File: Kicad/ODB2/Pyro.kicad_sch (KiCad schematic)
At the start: 35 parts

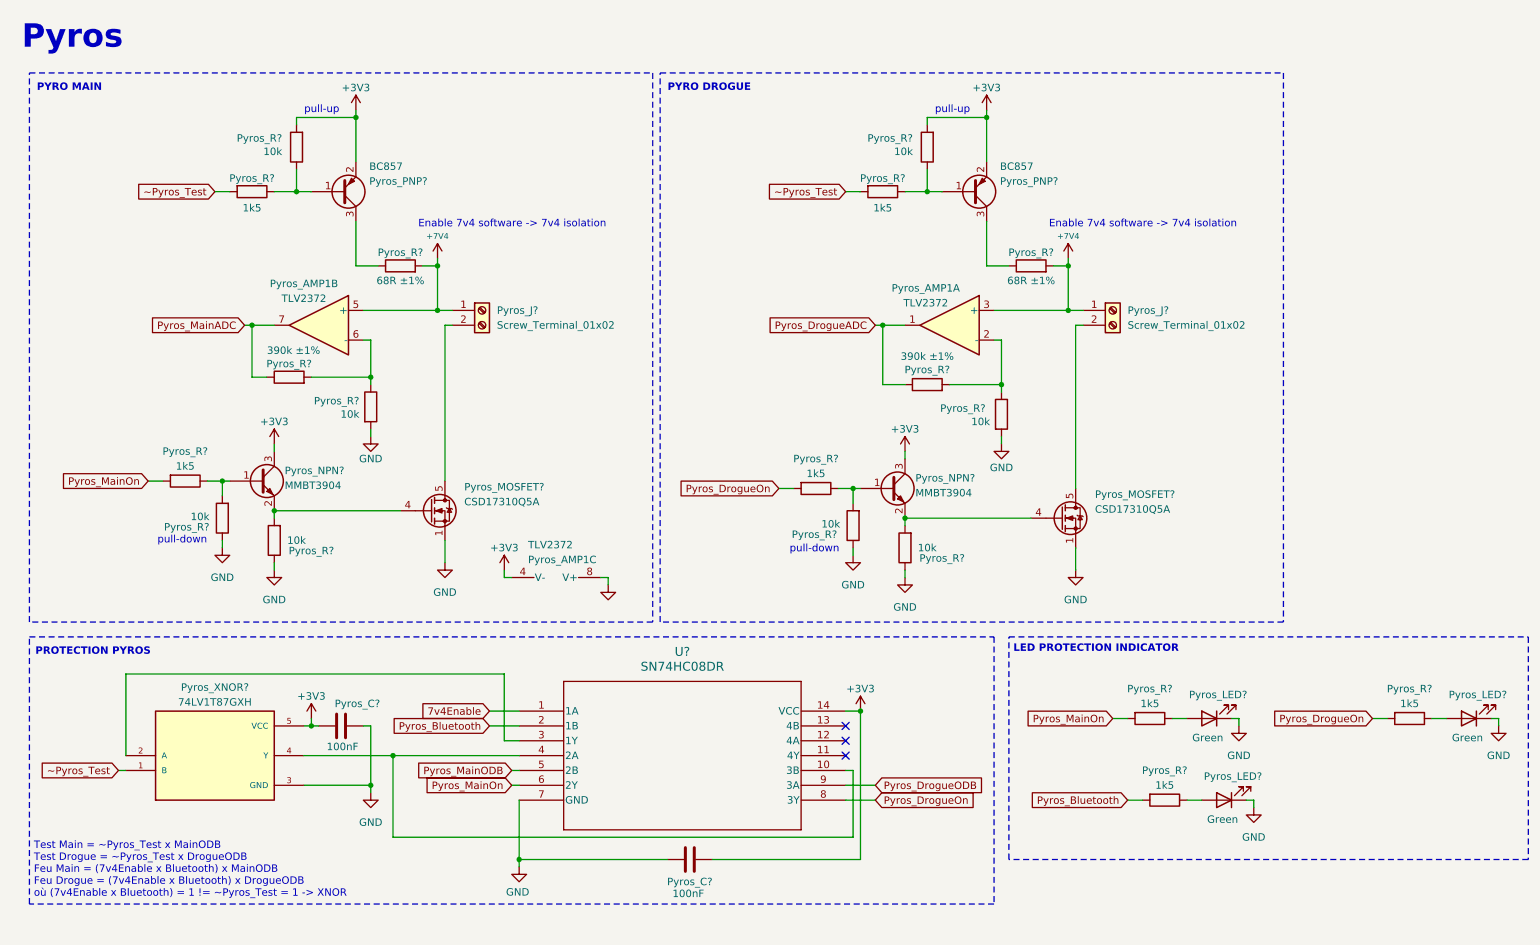
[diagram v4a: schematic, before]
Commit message: fix Labels + fix STM32 projet pinout
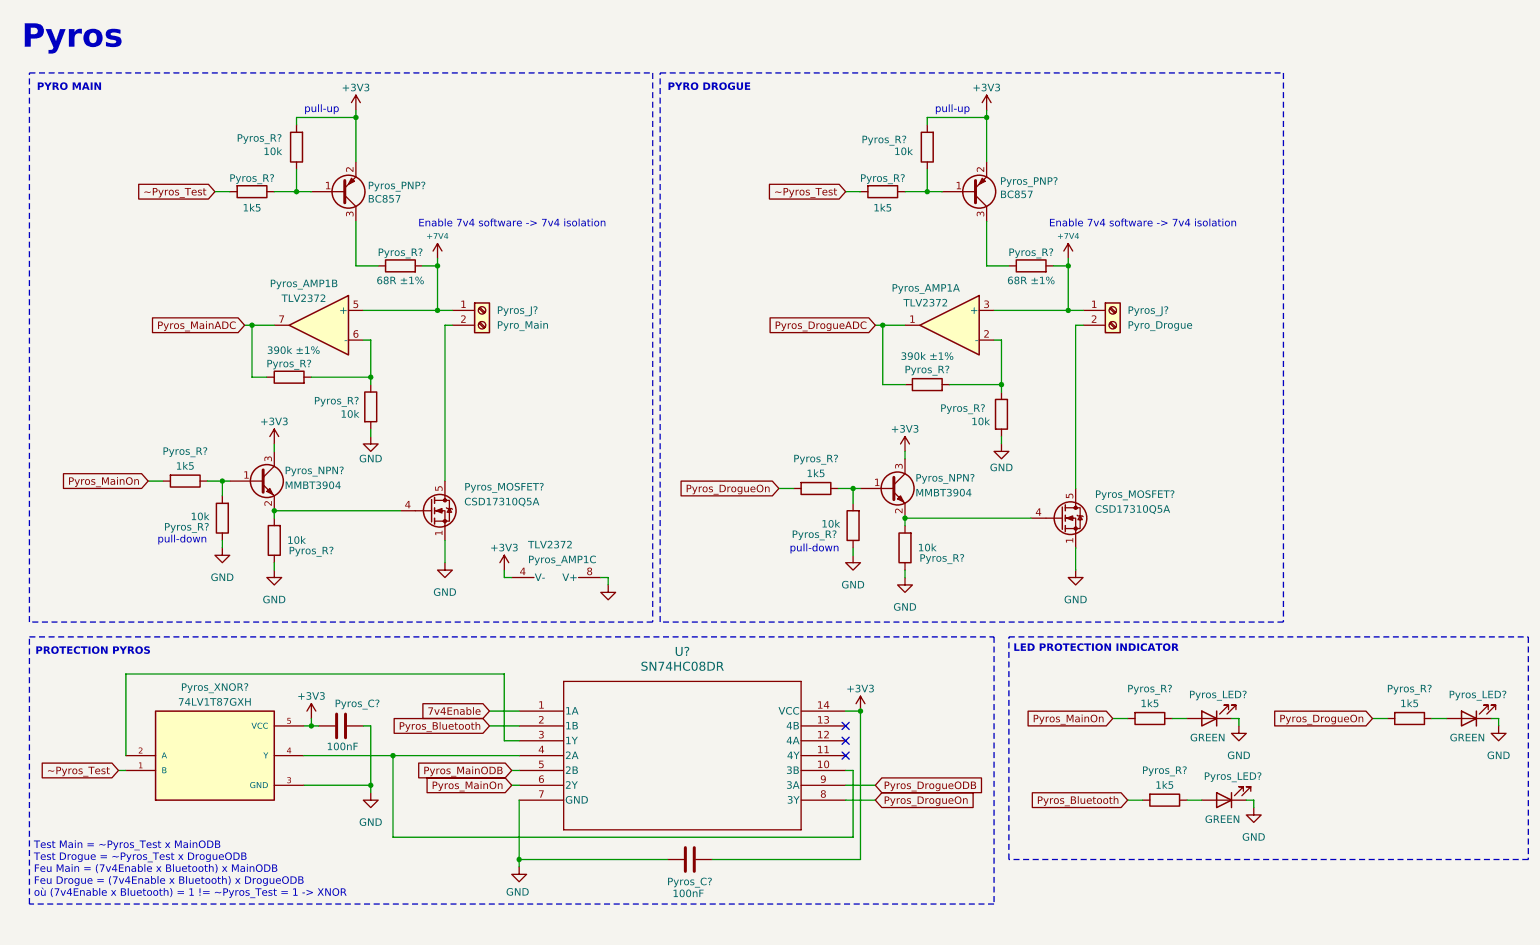
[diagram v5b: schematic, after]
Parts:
- Pyros_J?: value Screw_Terminal_01x02 -> Pyro_Drogue
- Pyros_J?: value Screw_Terminal_01x02 -> Pyro_Main
- Pyros_LED? (x3): value Green -> GREEN
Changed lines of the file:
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@@
 			)
 		)
-		(property "Value" "Green"
+		(property "Value" "GREEN"
 			(at 216.916 136.652 0)
 			(effects
@@
 		(dnp no)
 		(property "Reference" "Pyros_PNP?"
-			(at 73.406 41.402 0)
+			(at 73.152 42.164 0)
 			(effects
 				(font
@@
 		)
 		(property "Value" "BC857"
-			(at 73.406 38.862 0)
+			(at 73.152 44.45 0)
 			(effects
 				(font
@@
 			(project "ODB2"
 				(path "/4b06c5d1-aa8b-48ed-8972-b43a60cfab78/8ab7427e-7183-4caa-ac8a-08b0bd412372"
-					(reference "Pyros_R13")
+					(reference "Pyros_R16")
 					(unit 1)
 				)
@@
 			)
 		)
-		(property "Value" "Green"
+		(property "Value" "GREEN"
 			(at 219.456 150.622 0)
 			(effects
@@
 			(project "ODB2"
 				(path "/4b06c5d1-aa8b-48ed-8972-b43a60cfab78/8ab7427e-7183-4caa-ac8a-08b0bd412372"
-					(reference "Pyros_R18")
+					(reference "Pyros_R11")
 					(unit 1)
 				)
@@
 			(project "ODB2"
 				(path "/4b06c5d1-aa8b-48ed-8972-b43a60cfab78/8ab7427e-7183-4caa-ac8a-08b0bd412372"
-					(reference "Pyros_R9")
+					(reference "Pyros_R14")
 					(unit 1)
 				)
@@
 			(project "ODB2"
 				(path "/4b06c5d1-aa8b-48ed-8972-b43a60cfab78/8ab7427e-7183-4caa-ac8a-08b0bd412372"
-					(reference "Pyros_R11")
+					(reference "Pyros_R9")
 					(unit 1)
 				)
@@
 			(project "ODB2"
 				(path "/4b06c5d1-aa8b-48ed-8972-b43a60cfab78/8ab7427e-7183-4caa-ac8a-08b0bd412372"
-					(reference "Pyros_R15")
+					(reference "Pyros_R13")
 					(unit 1)
 				)
@@
 			(project "ODB2"
 				(path "/4b06c5d1-aa8b-48ed-8972-b43a60cfab78/8ab7427e-7183-4caa-ac8a-08b0bd412372"
-					(reference "Pyros_R10")
+					(reference "Pyros_R15")
 					(unit 1)
 				)
@@
 		)
 		(property "Value" "BC857"
-			(at 181.356 38.862 0)
+			(at 181.356 43.688 0)
 			(effects
 				(font
@@
 			)
 		)
-		(property "Value" "Screw_Terminal_01x02"
+		(property "Value" "Pyro_Drogue"
 			(at 203.2 66.0399 0)
 			(effects
@@
 			(project "ODB2"
 				(path "/4b06c5d1-aa8b-48ed-8972-b43a60cfab78/8ab7427e-7183-4caa-ac8a-08b0bd412372"
-					(reference "Pyros_J1")
+					(reference "Pyros_J2")
 					(unit 1)
 				)
@@
 			(project ""
 				(path "/4b06c5d1-aa8b-48ed-8972-b43a60cfab78/8ab7427e-7183-4caa-ac8a-08b0bd412372"
-					(reference "U12")
+					(reference "Pyros_AND1")
 					(unit 1)
 				)
@@
 		(dnp no)
 		(property "Reference" "Pyros_R?"
-			(at 162.56 34.036 0)
+			(at 161.544 34.29 0)
 			(effects
 				(font
@@
 			(project "ODB2"
 				(path "/4b06c5d1-aa8b-48ed-8972-b43a60cfab78/8ab7427e-7183-4caa-ac8a-08b0bd412372"
-					(reference "Pyros_R14")
+					(reference "Pyros_R10")
 					(unit 1)
 				)
@@
 			(project "ODB2"
 				(path "/4b06c5d1-aa8b-48ed-8972-b43a60cfab78/8ab7427e-7183-4caa-ac8a-08b0bd412372"
-					(reference "Pyros_R17")
+					(reference "Pyros_R18")
 					(unit 1)
 				)
@@
 			(project "ODB2"
 				(path "/4b06c5d1-aa8b-48ed-8972-b43a60cfab78/8ab7427e-7183-4caa-ac8a-08b0bd412372"
-					(reference "Pyros_R16")
+					(reference "Pyros_R17")
 					(unit 1)
 				)
@@
 			)
 		)
-		(property "Value" "Green"
+		(property "Value" "GREEN"
 			(at 261.366 136.652 0)
 			(effects
@@
 			)
 		)
-		(property "Value" "Screw_Terminal_01x02"
+		(property "Value" "Pyro_Main"
 			(at 95.25 66.0399 0)
 			(effects
@@
 			(project ""
 				(path "/4b06c5d1-aa8b-48ed-8972-b43a60cfab78/8ab7427e-7183-4caa-ac8a-08b0bd412372"
-					(reference "Pyros_J6")
+					(reference "Pyros_J1")
 					(unit 1)
 				)

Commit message: Fix somes issue
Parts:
- Pyros_C? (x2): footprint Capacitor_SMD:C_0805_2012Metric -> Capacitor_SMD:C_0603_1608Metric
- Pyros_LED? (x3): footprint LED_SMD:LED_0805_2012Metric -> LED_SMD:LED_0603_1608Metric
- Pyros_R? (x19): footprint Resistor_SMD:R_0805_2012Metric -> Resistor_SMD:R_0603_1608Metric
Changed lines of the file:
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@@
 			)
 		)
-		(property "Footprint" "LED_SMD:LED_0805_2012Metric"
+		(property "Footprint" "LED_SMD:LED_0603_1608Metric"
 			(at 217.17 133.35 0)
 			(effects
@@
 			)
 		)
-		(property "Footprint" "Resistor_SMD:R_0805_2012Metric"
+		(property "Footprint" "Resistor_SMD:R_0603_1608Metric"
 			(at 41.91 90.932 90)
 			(effects
@@
 			)
 		)
-		(property "Footprint" "Resistor_SMD:R_0805_2012Metric"
+		(property "Footprint" "Resistor_SMD:R_0603_1608Metric"
 			(at 166.878 104.14 90)
 			(effects
@@
 			)
 		)
-		(property "Footprint" "Resistor_SMD:R_0805_2012Metric"
+		(property "Footprint" "Resistor_SMD:R_0603_1608Metric"
 			(at 168.91 77.978 90)
 			(effects
@@
 			)
 		)
-		(property "Footprint" "Resistor_SMD:R_0805_2012Metric"
+		(property "Footprint" "Resistor_SMD:R_0603_1608Metric"
 			(at 59.69 76.708 90)
 			(effects
@@
 			)
 		)
-		(property "Footprint" "Resistor_SMD:R_0805_2012Metric"
+		(property "Footprint" "Resistor_SMD:R_0603_1608Metric"
 			(at 71.882 80.01 90)
 			(effects
@@
 			)
 		)
-		(property "Footprint" "Resistor_SMD:R_0805_2012Metric"
+		(property "Footprint" "Resistor_SMD:R_0603_1608Metric"
 			(at 50.038 99.06 90)
 			(effects
@@
 			)
 		)
-		(property "Footprint" "LED_SMD:LED_0805_2012Metric"
+		(property "Footprint" "LED_SMD:LED_0603_1608Metric"
 			(at 219.71 147.32 0)
 			(effects
@@
 			)
 		)
-		(property "Footprint" "Capacitor_SMD:C_0805_2012Metric"
+		(property "Footprint" "Capacitor_SMD:C_0603_1608Metric"
 			(at 64.77 135.5852 0)
 			(effects
@@
 			)
 		)
-		(property "Footprint" "Resistor_SMD:R_0805_2012Metric"
+		(property "Footprint" "Resistor_SMD:R_0603_1608Metric"
 			(at 186.69 57.658 90)
 			(effects
@@
 			)
 		)
-		(property "Footprint" "Resistor_SMD:R_0805_2012Metric"
+		(property "Footprint" "Resistor_SMD:R_0603_1608Metric"
 			(at 149.86 92.202 90)
 			(effects
@@
 			)
 		)
-		(property "Footprint" "Resistor_SMD:R_0805_2012Metric"
+		(property "Footprint" "Resistor_SMD:R_0603_1608Metric"
 			(at 161.29 41.402 90)
 			(effects
@@
 			)
 		)
-		(property "Footprint" "Resistor_SMD:R_0805_2012Metric"
+		(property "Footprint" "Resistor_SMD:R_0603_1608Metric"
 			(at 179.832 81.28 90)
 			(effects
@@
 			)
 		)
-		(property "Footprint" "Resistor_SMD:R_0805_2012Metric"
+		(property "Footprint" "Resistor_SMD:R_0603_1608Metric"
 			(at 58.928 102.87 90)
 			(effects
@@
 			)
 		)
-		(property "Footprint" "Resistor_SMD:R_0805_2012Metric"
+		(property "Footprint" "Resistor_SMD:R_0603_1608Metric"
 			(at 157.988 100.33 90)
 			(effects
@@
 			)
 		)
-		(property "Footprint" "Resistor_SMD:R_0805_2012Metric"
+		(property "Footprint" "Resistor_SMD:R_0603_1608Metric"
 			(at 53.34 41.402 90)
 			(effects
@@
 			)
 		)
-		(property "Footprint" "Resistor_SMD:R_0805_2012Metric"
+		(property "Footprint" "Resistor_SMD:R_0603_1608Metric"
 			(at 78.74 57.658 90)
 			(effects
@@
 			)
 		)
-		(property "Footprint" "Resistor_SMD:R_0805_2012Metric"
+		(property "Footprint" "Resistor_SMD:R_0603_1608Metric"
 			(at 209.55 145.542 90)
 			(effects
@@
 			)
 		)
-		(property "Footprint" "Resistor_SMD:R_0805_2012Metric"
+		(property "Footprint" "Resistor_SMD:R_0603_1608Metric"
 			(at 170.688 35.56 90)
 			(effects
@@
 			)
 		)
-		(property "Footprint" "Resistor_SMD:R_0805_2012Metric"
+		(property "Footprint" "Resistor_SMD:R_0603_1608Metric"
 			(at 251.46 131.572 90)
 			(effects
@@
 			)
 		)
-		(property "Footprint" "Resistor_SMD:R_0805_2012Metric"
+		(property "Footprint" "Resistor_SMD:R_0603_1608Metric"
 			(at 207.01 131.572 90)
 			(effects
@@
 			)
 		)
-		(property "Footprint" "LED_SMD:LED_0805_2012Metric"
+		(property "Footprint" "LED_SMD:LED_0603_1608Metric"
 			(at 261.62 133.35 0)
 			(effects
@@
 			)
 		)
-		(property "Footprint" "Capacitor_SMD:C_0805_2012Metric"
+		(property "Footprint" "Capacitor_SMD:C_0603_1608Metric"
 			(at 124.46 158.4452 0)
 			(effects
@@
 			)
 		)
-		(property "Footprint" "Resistor_SMD:R_0805_2012Metric"
+		(property "Footprint" "Resistor_SMD:R_0603_1608Metric"
 			(at 62.738 35.56 90)
 			(effects

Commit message: Updated pcb
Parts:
- removed unit 1 of Pyros_AMP1
- removed Pyros_PNP?: BC857, Package_TO_SOT_SMD:SOT-23, symbol Transistor_BJT:BC857
- removed Pyros_R?: 390k ±1%, Resistor_SMD:R_0603_1608Metric, symbol Device:R
- removed Pyros_R?: 68R ±1%, Resistor_SMD:R_0603_1608Metric, symbol Device:R
- removed Pyros_R?: 1k5, Resistor_SMD:R_0603_1608Metric, symbol Device:R
- removed Pyros_R? (x2): 10k, Resistor_SMD:R_0603_1608Metric, symbol Device:R
